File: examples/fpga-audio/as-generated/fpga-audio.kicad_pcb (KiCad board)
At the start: 4 copper layers, 76 x 58 mm, 36 parts, among them J1 3V3 IN, J2 AUDIO OUT, J3 SPI PROG, U1 iCE40UP5K, U2 PCM5102A, U3 AP2112K-1.2, U4 W25Q32JV, X1 12MHz

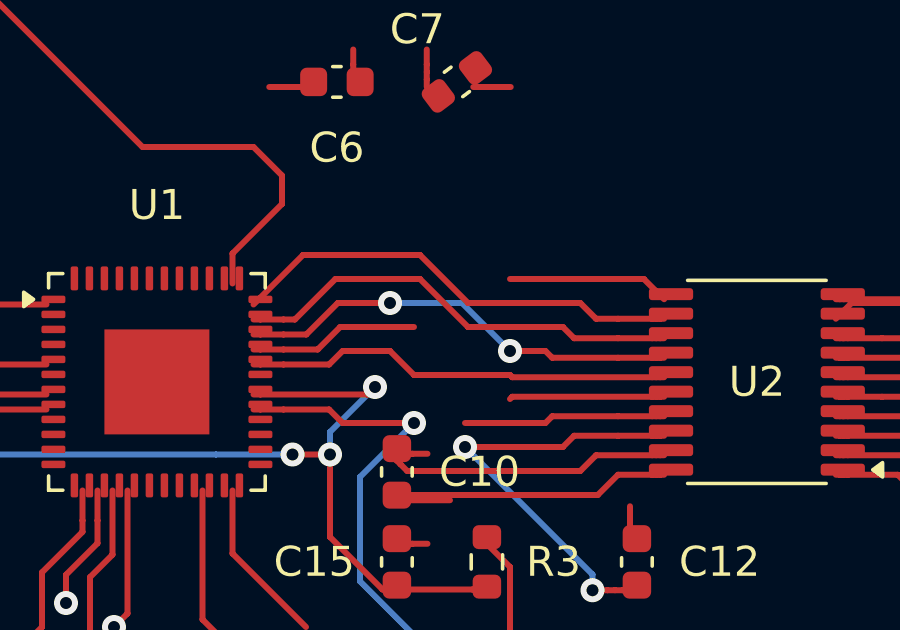
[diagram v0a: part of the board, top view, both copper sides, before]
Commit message: fix(examples): refine local escapes and enforce complete cross-version golden checks
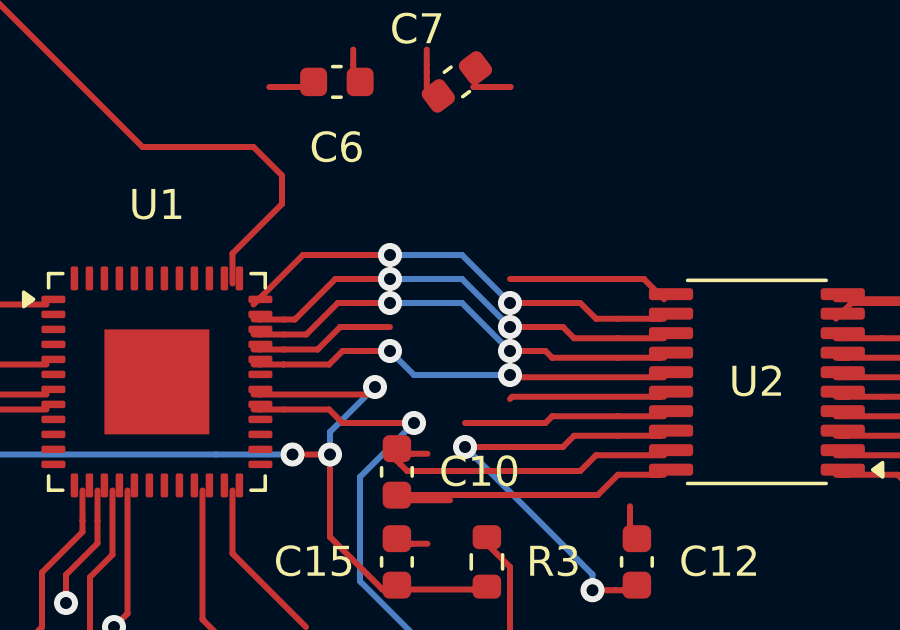
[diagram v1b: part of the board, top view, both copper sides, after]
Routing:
- net +3V3: track 122.9 -> 122.1 mm
- net /I2S_BCK: vias 0 -> 2
- net /I2S_SCK: vias 0 -> 2
- net /I2S_LRCK: vias 0 -> 2
